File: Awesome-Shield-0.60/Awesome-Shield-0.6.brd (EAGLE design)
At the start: 51 x 55 mm, 21 parts, among them J1 PORT1, J2 PORT2, J3 PORT3, SW1 SPST_TACT-EVQQ2, SW2 DPDT, U1 LIGHTSENSORTEMT6000

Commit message: close #39 close #41 close #42
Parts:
- flipped SJ1 to the bottom
- flipped SJ2 to the bottom
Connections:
- net D3: now also J2.2
- net D4: no longer J2.2
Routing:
- net D3: track 0.00 -> 61.2 mm, vias 0 -> 1
- net D4: track 58.8 -> 0.00 mm, vias 1 -> 0
- net GND: track 16.1 -> 18.5 mm
- net SCL: track 90.4 -> 89.5 mm, vias 2 -> 1
- net SDA: track 91.7 -> 91.4 mm, vias 3 -> 2

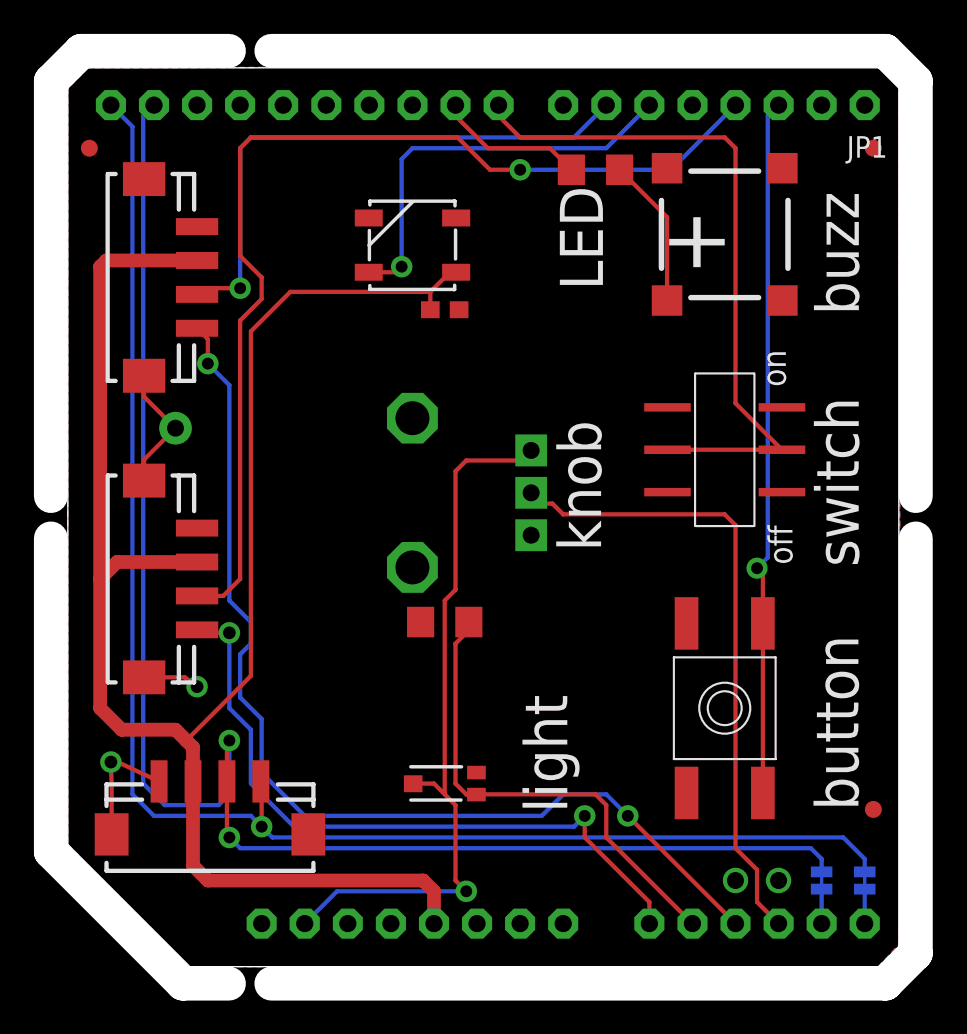
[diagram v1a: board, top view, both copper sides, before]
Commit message: nudged components to provide more optimal spaces for labels in silkscreen
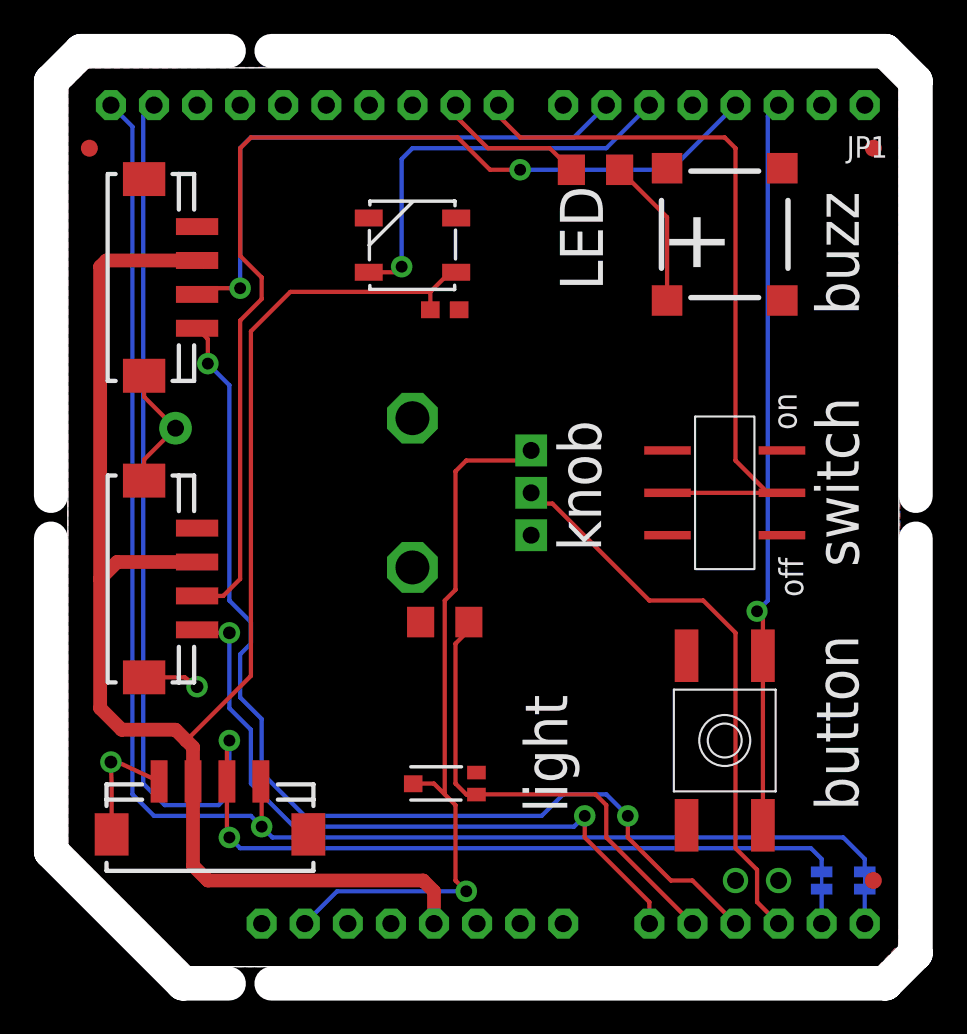
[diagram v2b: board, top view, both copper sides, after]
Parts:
- moved FID3 4.19 mm to (47.5, 5.08)
- moved SW2 2.54 mm to (38.7, 27.9)
- moved SW1 1.90 mm to (38.7, 13.3)
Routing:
- net A3: track 37.4 -> 33.7 mm
- net D8: track 41.1 -> 44.1 mm
- net D2: track 41.2 -> 43.1 mm
- net A2: track 61.0 -> 61.7 mm

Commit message: moved photodiode to make space for graphic
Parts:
- moved R6 5.12 mm to (17.1, 19.7)
- moved U1 2.62 mm to (21.6, 13.3), turned to 270 degrees
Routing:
- net IOREF: track 43.0 -> 45.4 mm
- net A1: track 28.4 -> 29.6 mm
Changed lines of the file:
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@@
 <text x="46.615" y="9.211" size="2.54" layer="25" font="vector" rot="R90">button</text>
 <text x="28.905" y="32.213" size="2.54" layer="25" font="vector" rot="R270">knob</text>
-<text x="26.912" y="16.031" size="2.54" layer="25" font="vector" rot="R270">light</text>
+<text x="23.737" y="17.936" size="2.54" layer="25" font="vector" rot="R270">light</text>
 <text x="46.64210625" y="38.42526875" size="2.54" layer="25" font="vector" rot="SR90">buzz</text>
 <text x="29.013" y="46.034" size="2.54" layer="25" font="vector" rot="R270">LED</text>
@@
 </autorouter>
 <elements>
-<element name="R6" library="rcl" package="R1206" value="10K" x="22.225" y="20.32" smashed="yes" rot="R180"/>
+<element name="R6" library="rcl" package="R1206" value="10K" x="17.145" y="19.685" smashed="yes" rot="R180"/>
 <element name="SW1" library="adafruit" package="EVQ-Q2" value="SPST_TACT-EVQQ2" x="38.735" y="13.335" smashed="yes" rot="R270"/>
 <element name="SJ1" library="SparkFun-Passives" package="PAD-JUMPER-2-NC_BY_TRACE_YES_SILK" value="JUMPER-PAD-2-NC_BY_TRACE" x="44.45" y="5.08" smashed="yes" rot="MR270"/>
@@
 <element name="FID3" library="SparkFun-Aesthetics" package="FIDUCIAL-1X2" value="FIDUCIAL1X2" x="47.498" y="5.08"/>
 <element name="FID4" library="SparkFun-Aesthetics" package="FIDUCIAL-1X2" value="FIDUCIAL1X2" x="1.27" y="48.26"/>
-<element name="U1" library="SparkFun-Sensors" package="TEMT6000-SEN" value="LIGHTSENSORTEMT6000" x="22.225" y="10.795" smashed="yes" rot="R180"/>
+<element name="U1" library="SparkFun-Sensors" package="TEMT6000-SEN" value="LIGHTSENSORTEMT6000" x="21.59" y="13.335" smashed="yes" rot="R270"/>
 <element name="JP4" library="adafruit" package="1X10-BIG" value="PINHD-1X10" x="13.97" y="50.8" smashed="yes" rot="R180"/>
 <element name="JP1" library="adafruit" package="1X08-CLEANBIG" value="" x="38.1" y="50.8" rot="R180"/>
@@
 <wire x1="31.75" y1="7.62" x2="31.75" y2="9.525" width="0.254" layer="1"/>
 <wire x1="31.75" y1="9.525" x2="31.115" y2="10.16" width="0.254" layer="1"/>
-<wire x1="22.86" y1="10.795" x2="23.51" y2="10.145" width="0.254" layer="1"/>
-<wire x1="23.51" y1="10.145" x2="24.095" y2="10.145" width="0.254" layer="1"/>
-<wire x1="22.86" y1="10.795" x2="22.86" y2="19.05" width="0.254" layer="1"/>
-<wire x1="22.86" y1="19.05" x2="23.647" y2="19.837" width="0.254" layer="1"/>
-<wire x1="23.647" y1="19.837" x2="23.647" y2="20.32" width="0.254" layer="1"/>
-<wire x1="31.115" y1="10.16" x2="24.11" y2="10.16" width="0.254" layer="1"/>
-<wire x1="24.11" y1="10.16" x2="24.095" y2="10.145" width="0.254" layer="1"/>
+<wire x1="31.115" y1="10.16" x2="25.4" y2="10.16" width="0.254" layer="1"/>
+<wire x1="22.225" y1="15.875" x2="22.225" y2="13.335" width="0.254" layer="1"/>
+<wire x1="22.225" y1="13.335" x2="25.4" y2="10.16" width="0.254" layer="1"/>
+<wire x1="21.59" y1="16.51" x2="22.225" y2="15.875" width="0.254" layer="1"/>
+<wire x1="18.567" y1="18.898" x2="18.567" y2="19.685" width="0.254" layer="1"/>
+<wire x1="21.59" y1="16.51" x2="20.32" y2="16.51" width="0.254" layer="1"/>
+<wire x1="20.32" y1="16.51" x2="18.567" y2="18.263" width="0.254" layer="1"/>
+<wire x1="18.567" y1="18.263" x2="18.567" y2="19.685" width="0.254" layer="1"/>
+<wire x1="22.225" y1="15.875" x2="22.24" y2="15.205" width="0" layer="19" extent="1-1"/>
 </signal>
 <signal name="GND">
@@
 <wire x1="15.875" y1="4.445" x2="23.495" y2="4.445" width="0.254" layer="16"/>
 <via x="23.495" y="4.445" extent="1-16" drill="0.7" diameter="1.27"/>
-<wire x1="22.225" y1="10.16" x2="22.225" y2="21.59" width="0.254" layer="1"/>
-<wire x1="22.225" y1="21.59" x2="22.86" y2="22.225" width="0.254" layer="1"/>
-<wire x1="22.86" y1="22.225" x2="22.86" y2="29.21" width="0.254" layer="1"/>
-<wire x1="22.86" y1="29.21" x2="23.495" y2="29.845" width="0.254" layer="1"/>
-<wire x1="23.495" y1="29.845" x2="26.725" y2="29.845" width="0.254" layer="1"/>
 <wire x1="26.725" y1="29.845" x2="27.32" y2="30.44" width="0.254" layer="1"/>
-<wire x1="23.495" y1="4.445" x2="22.86" y2="5.08" width="0.254" layer="1"/>
-<wire x1="22.86" y1="5.08" x2="22.86" y2="9.525" width="0.254" layer="1"/>
-<wire x1="22.86" y1="9.525" x2="22.225" y2="10.16" width="0.254" layer="1"/>
-<wire x1="22.225" y1="10.16" x2="21.59" y2="10.795" width="0.254" layer="1"/>
-<wire x1="21.59" y1="10.795" x2="20.375" y2="10.795" width="0.254" layer="1"/>
-<wire x1="20.375" y1="10.795" x2="20.365" y2="10.785" width="0.254" layer="1"/>
+<wire x1="26.725" y1="29.845" x2="22.86" y2="29.845" width="0.254" layer="1"/>
+<wire x1="22.86" y1="29.845" x2="17.145" y2="24.13" width="0.254" layer="1"/>
+<wire x1="19.685" y1="14.605" x2="21.6" y2="12.69" width="0.254" layer="1"/>
+<wire x1="21.6" y1="12.69" x2="21.6" y2="11.475" width="0.254" layer="1"/>
+<wire x1="23.495" y1="4.445" x2="21.6" y2="6.34" width="0.254" layer="1"/>
+<wire x1="21.6" y1="6.34" x2="21.6" y2="11.475" width="0.254" layer="1"/>
+<wire x1="17.145" y1="24.13" x2="17.145" y2="18.415" width="0.254" layer="1"/>
+<wire x1="17.145" y1="18.415" x2="19.685" y2="15.875" width="0.254" layer="1"/>
+<wire x1="19.685" y1="15.875" x2="19.685" y2="14.605" width="0.254" layer="1"/>
 </signal>
 <signal name="+3V3">

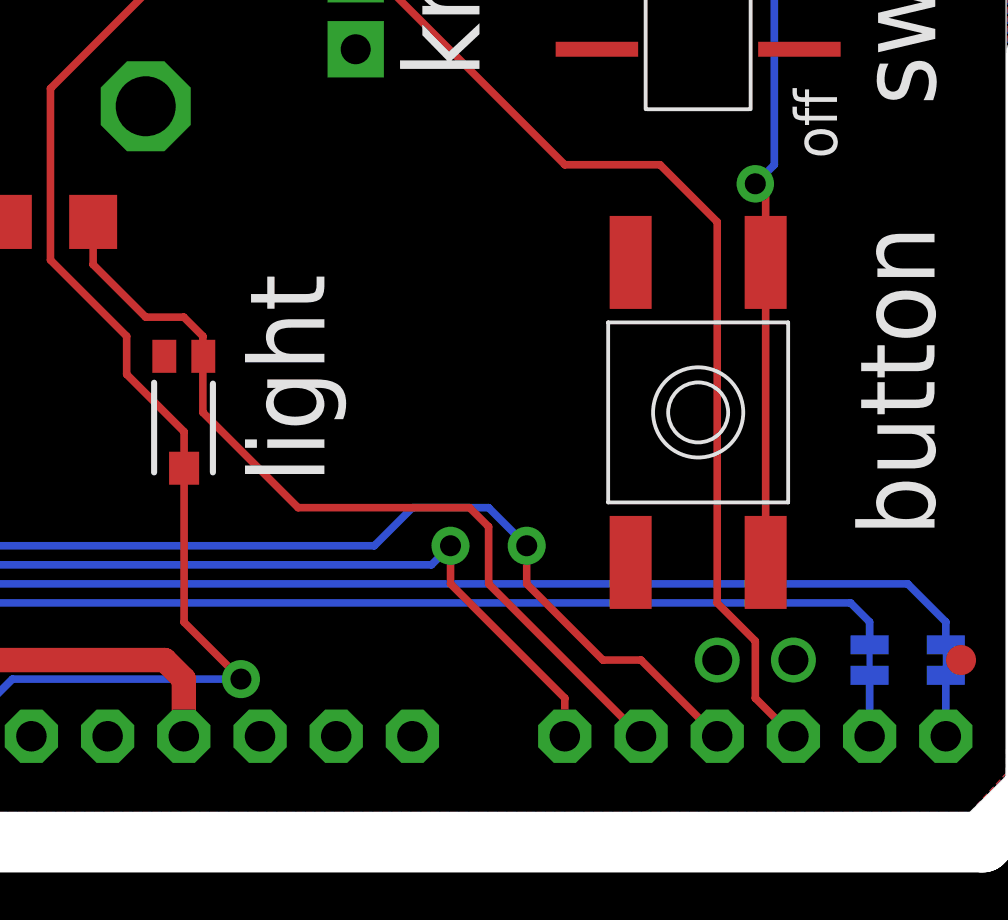
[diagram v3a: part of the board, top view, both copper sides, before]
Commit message: moved button to make more room for graphic
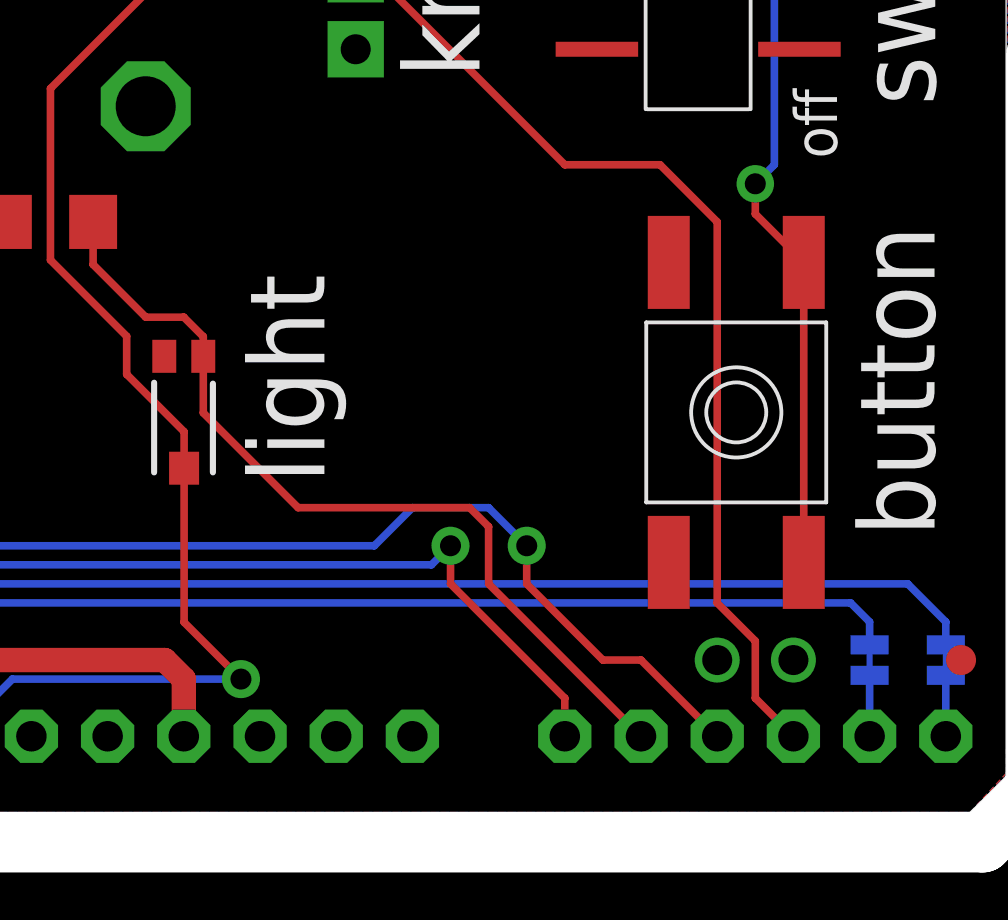
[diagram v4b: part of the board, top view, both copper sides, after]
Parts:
- moved SW1 1.27 mm to (40.0, 13.3)
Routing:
- net D2: track 43.1 -> 43.7 mm
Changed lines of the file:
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@@
 <elements>
 <element name="R6" library="rcl" package="R1206" value="10K" x="17.145" y="19.685" smashed="yes" rot="R180"/>
-<element name="SW1" library="adafruit" package="EVQ-Q2" value="SPST_TACT-EVQQ2" x="38.735" y="13.335" smashed="yes" rot="R270"/>
+<element name="SW1" library="adafruit" package="EVQ-Q2" value="SPST_TACT-EVQQ2" x="40.005" y="13.335" smashed="yes" rot="R270"/>
 <element name="SJ1" library="SparkFun-Passives" package="PAD-JUMPER-2-NC_BY_TRACE_YES_SILK" value="JUMPER-PAD-2-NC_BY_TRACE" x="44.45" y="5.08" smashed="yes" rot="MR270"/>
 <element name="SJ2" library="SparkFun-Passives" package="PAD-JUMPER-2-NC_BY_TRACE_YES_SILK" value="JUMPER-PAD-2-NC_BY_TRACE" x="46.99" y="5.08" smashed="yes" rot="MR270"/>
@@
 <contactref element="R6" pad="1"/>
 <contactref element="U1" pad="EMITTER"/>
-<wire x1="36.83" y1="2.54" x2="31.75" y2="7.62" width="0.254" layer="1"/>
-<wire x1="31.75" y1="7.62" x2="31.75" y2="9.525" width="0.254" layer="1"/>
-<wire x1="31.75" y1="9.525" x2="31.115" y2="10.16" width="0.254" layer="1"/>
-<wire x1="31.115" y1="10.16" x2="25.4" y2="10.16" width="0.254" layer="1"/>
-<wire x1="22.225" y1="15.875" x2="22.225" y2="13.335" width="0.254" layer="1"/>
-<wire x1="22.225" y1="13.335" x2="25.4" y2="10.16" width="0.254" layer="1"/>
-<wire x1="21.59" y1="16.51" x2="22.225" y2="15.875" width="0.254" layer="1"/>
 <wire x1="18.567" y1="18.898" x2="18.567" y2="19.685" width="0.254" layer="1"/>
 <wire x1="21.59" y1="16.51" x2="20.32" y2="16.51" width="0.254" layer="1"/>
 <wire x1="20.32" y1="16.51" x2="18.567" y2="18.263" width="0.254" layer="1"/>
 <wire x1="18.567" y1="18.263" x2="18.567" y2="19.685" width="0.254" layer="1"/>
-<wire x1="22.225" y1="15.875" x2="22.24" y2="15.205" width="0" layer="19" extent="1-1"/>
+<wire x1="22.24" y1="15.205" x2="22.24" y2="15.86" width="0.254" layer="1"/>
+<wire x1="22.24" y1="15.86" x2="21.59" y2="16.51" width="0.254" layer="1"/>
+<wire x1="22.24" y1="15.205" x2="22.24" y2="13.32" width="0.254" layer="1"/>
+<wire x1="22.24" y1="13.32" x2="25.4" y2="10.16" width="0.254" layer="1"/>
+<wire x1="25.4" y1="10.16" x2="31.115" y2="10.16" width="0.254" layer="1"/>
+<wire x1="31.115" y1="10.16" x2="31.75" y2="9.525" width="0.254" layer="1"/>
+<wire x1="31.75" y1="9.525" x2="31.75" y2="7.62" width="0.254" layer="1"/>
+<wire x1="31.75" y1="7.62" x2="36.83" y2="2.54" width="0.254" layer="1"/>
 </signal>
 <signal name="GND">
@@
 <contactref element="JP1" pad="3"/>
 <via x="40.64" y="20.955" extent="1-16" drill="0.7" diameter="1.25"/>
-<wire x1="40.985" y1="8.335" x2="40.985" y2="18.335" width="0.254" layer="1"/>
+<wire x1="42.255" y1="8.335" x2="42.255" y2="18.335" width="0.254" layer="1"/>
 <wire x1="41.91" y1="50.8" x2="41.275" y2="50.165" width="0.254" layer="16"/>
 <wire x1="41.275" y1="50.165" x2="41.275" y2="21.59" width="0.254" layer="16"/>
 <wire x1="40.64" y1="20.955" x2="41.275" y2="21.59" width="0.254" layer="16"/>
-<wire x1="40.985" y1="18.335" x2="40.985" y2="20.61" width="0.254" layer="1"/>
-<wire x1="40.985" y1="20.61" x2="40.64" y2="20.955" width="0.254" layer="1"/>
+<wire x1="42.255" y1="18.335" x2="40.64" y2="19.95" width="0.254" layer="1"/>
+<wire x1="40.64" y1="19.95" x2="40.64" y2="20.955" width="0.254" layer="1"/>
 </signal>
 <signal name="D6">
